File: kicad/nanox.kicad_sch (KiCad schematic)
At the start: 139 parts, among them P1 likely an ESD protection diod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, P2 likely an ESD protection diod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, P3 likely an ESD protection diod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, P4 likely an ESD protection diod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, P5 likely an ESD protection diod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, SW1 push button, left, SW2 push button, right, X1 ?, X10 TI TLV61046A boost converter 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, X11 unknown, marked AF, likely a 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, X12 unknown, likely a P-channel M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, X2 likely an N-channel MOSFET: t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, X3 likely an N-channel MOSFET: t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, X4 ?, X5 ?, X6 ?, X7 ?, X8 ?, X9 NXP PMBZ5246B 16 V Zener diod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, Y1 crystal, likely the 32 MHz HSE

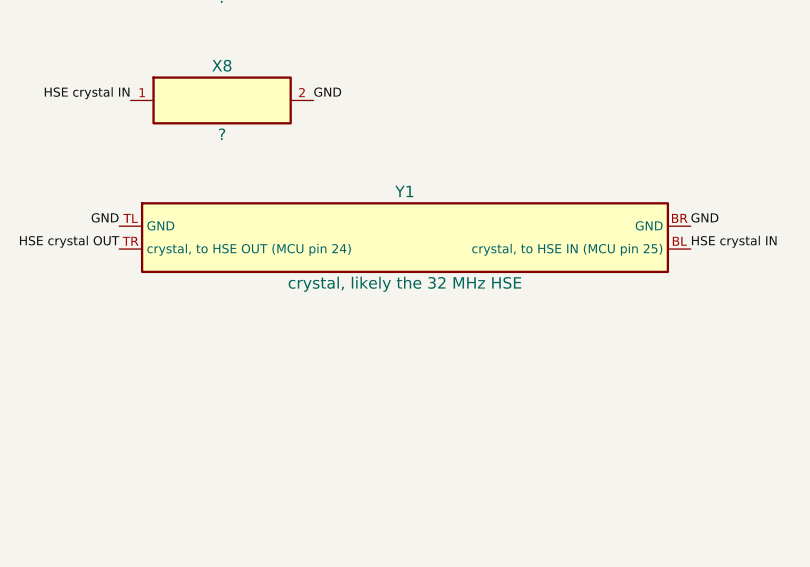
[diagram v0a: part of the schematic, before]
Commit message: Read Y1's marking as 32000 K145 Y: the 32 MHz HSE crystal, confirmed
Co-Authored-By: Claude Opus 5.5 <noreply@anthropic.com>
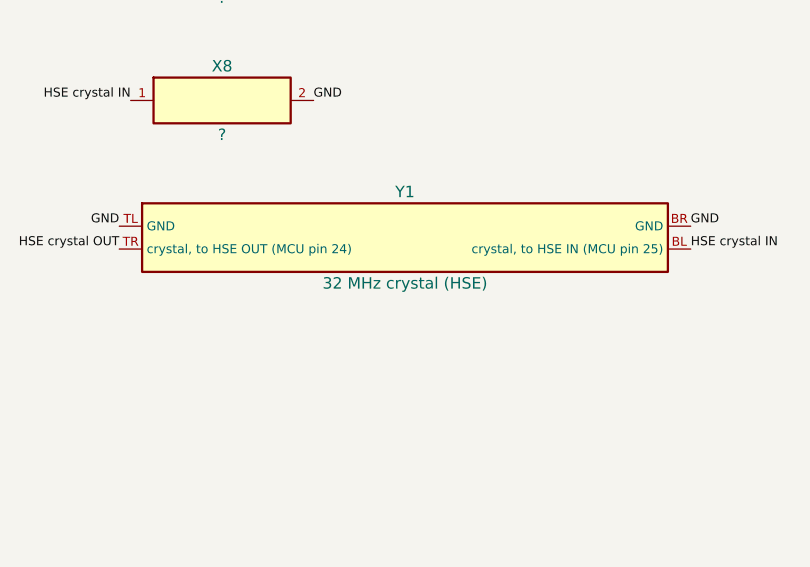
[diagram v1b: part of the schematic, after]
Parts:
- Y1: value crystal, likely the 32 MHz HSE -> 32 MHz crystal (HSE)
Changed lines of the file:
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@@
  (symbol (lib_id "nanox:Y1") (at 541.02 172.72 0) (unit 1) (in_bom yes) (on_board yes) (dnp no)
   (property "Reference" "Y1" (at 541.02 167.64 0) (effects (font (size 1.27 1.27))))
-  (property "Value" "crystal, likely the 32 MHz HSE" (at 541.02 177.80 0) (effects (font (size 1.27 1.27))))
+  (property "Value" "32 MHz crystal (HSE)" (at 541.02 177.80 0) (effects (font (size 1.27 1.27))))
   (property "Footprint" "" (at 541.02 172.72 0) (effects (font (size 1.27 1.27)) hide))
   (property "Description" "4 corner pads, ~2.0 x 1.6 mm" (at 541.02 172.72 0) (effects (font (size 1.27 1.27)) hide))

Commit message: Add the empty LSE crystal footprints as not-populated parts
The MCU's low-speed clock traces end on footprints that are left empty on
the real board: bare, solder-tinned pads for a 32.768 kHz crystal (Y2)
and its two load capacitors (C38, C39). They are now in the model, marked
DNP and excluded from the BOM in KiCad, with no 3D body, so the LSE nets
end on them and the viewers show the bare pads. The MCU must run its RTC
from its internal oscillator instead.

Co-Authored-By: Claude Opus 5.5 <noreply@anthropic.com>
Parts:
- added C38: not populated: LSE load capacitor, symbol nanox:C38
- added C39: not populated: LSE load capacitor, symbol nanox:C39
- added Y2: not populated: 32.768 kHz crystal (LSE), symbol nanox:Y2
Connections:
- net LSE crystal IN: now also C38.1, Y2.1 (LSE IN)
- net LSE crystal OUT: now also C39.1, Y2.2 (LSE OUT)
- no-connect marks 72 -> 74
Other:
- moved on the sheet: C5, C6, C7, C8, C9, L1, MCU1, P1, P2, P3, P4, P5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

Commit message: Wire L1 into the OLED boost converter and close the loose resistor and capacitor ends
- L1 gets its two pads: VIN (the pad-19 supply) and the TLV61046A's SW pin
- R24 runs to the +3.3V via below it: a pull-up on OLED SPI CS
- the +3.3V trace by R18 is straightened onto its pad: a pull-up on the
  charger's ST2 status output
- C1, C23, C24, R8 and R28 get their ground ends

Co-Authored-By: Claude Opus 5.5 <noreply@anthropic.com>
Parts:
- L1: value unknown, likely a shielded power inductor -> power inductor of the OLED boost converter
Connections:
- net +3.3V rail: now also R18.2, R24.2
- net GND: now also C1.2, C23.1, C24.1, R28.1, R8.2
- net Left button power (pad 19): now also L1.1 (VIN)
- net OLED boost SW: now also L1.2 (SW)
- no-connect marks 74 -> 67
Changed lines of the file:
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@@
  )
  (label "VBUS" (at 25.40 99.06 180) (effects (font (size 1.0 1.0)) (justify right bottom)))
- (no_connect (at 45.72 99.06))
+ (label "GND" (at 45.72 99.06 0) (effects (font (size 1.0 1.0)) (justify left bottom)))
  (symbol (lib_id "nanox:C10") (at 35.56 114.30 0) (unit 1) (in_bom yes) (on_board yes) (dnp no)
   (property "Reference" "C10" (at 35.56 110.49 0) (effects (font (size 1.27 1.27))))
@@
   (instances (project "nanox" (path "/9fc871f3-1e36-5a01-9359-e2a20c86f96f" (reference "C23") (unit 1))))
  )
- (no_connect (at 76.20 43.18))
+ (label "GND" (at 76.20 43.18 180) (effects (font (size 1.0 1.0)) (justify right bottom)))
  (label "+3.3V rail" (at 96.52 43.18 0) (effects (font (size 1.0 1.0)) (justify left bottom)))
  (symbol (lib_id "nanox:C24") (at 86.36 58.42 0) (unit 1) (in_bom yes) (on_board yes) (dnp no)
@@
   (instances (project "nanox" (path "/9fc871f3-1e36-5a01-9359-e2a20c86f96f" (reference "C24") (unit 1))))
  )
- (no_connect (at 76.20 58.42))
+ (label "GND" (at 76.20 58.42 180) (effects (font (size 1.0 1.0)) (justify right bottom)))
  (label "+3.3V rail" (at 96.52 58.42 0) (effects (font (size 1.0 1.0)) (justify left bottom)))
  (symbol (lib_id "nanox:C28") (at 86.36 73.66 0) (unit 1) (in_bom yes) (on_board yes) (dnp no)
@@
  (symbol (lib_id "nanox:L1") (at 137.16 73.66 0) (unit 1) (in_bom yes) (on_board yes) (dnp no)
   (property "Reference" "L1" (at 137.16 69.85 0) (effects (font (size 1.27 1.27))))
-  (property "Value" "unknown, likely a shielded power inductor" (at 137.16 77.47 0) (effects (font (size 1.27 1.27))))
+  (property "Value" "power inductor of the OLED boost converter" (at 137.16 77.47 0) (effects (font (size 1.27 1.27))))
   (property "Footprint" "" (at 137.16 73.66 0) (effects (font (size 1.27 1.27)) hide))
-  (property "Description" "~4.8 mm square metal" (at 137.16 73.66 0) (effects (font (size 1.27 1.27)) hide))
+  (property "Description" "~4.8 mm square metal, 2 pads" (at 137.16 73.66 0) (effects (font (size 1.27 1.27)) hide))
+  (pin "1")
+  (pin "2")
   (instances (project "nanox" (path "/9fc871f3-1e36-5a01-9359-e2a20c86f96f" (reference "L1") (unit 1))))
  )
+ (label "Left button power (pad 19)" (at 127.00 73.66 180) (effects (font (size 1.0 1.0)) (justify right bottom)))
+ (label "OLED boost SW" (at 147.32 73.66 0) (effects (font (size 1.0 1.0)) (justify left bottom)))
  (symbol (lib_id "nanox:MCU1") (at 142.24 119.38 0) (unit 1) (in_bom yes) (on_board yes) (dnp no)
   (property "Reference" "MCU1" (at 142.24 85.09 0) (effects (font (size 1.27 1.27))))
@@
  )
  (label "Charger ST2" (at 185.42 185.42 180) (effects (font (size 1.0 1.0)) (justify right bottom)))
- (no_connect (at 205.74 185.42))
+ (label "+3.3V rail" (at 205.74 185.42 0) (effects (font (size 1.0 1.0)) (justify left bottom)))
  (symbol (lib_id "nanox:R19") (at 195.58 200.66 0) (unit 1) (in_bom yes) (on_board yes) (dnp no)
   (property "Reference" "R19" (at 195.58 196.85 0) (effects (font (size 1.27 1.27))))
@@
  )
  (label "OLED SPI CS" (at 185.42 276.86 180) (effects (font (size 1.0 1.0)) (justify right bottom)))
- (no_connect (at 205.74 276.86))
+ (label "+3.3V rail" (at 205.74 276.86 0) (effects (font (size 1.0 1.0)) (justify left bottom)))
  (symbol (lib_id "nanox:R25") (at 195.58 292.10 0) (unit 1) (in_bom yes) (on_board yes) (dnp no)
   (property "Reference" "R25" (at 195.58 288.29 0) (effects (font (size 1.27 1.27))))
@@
   (instances (project "nanox" (path "/9fc871f3-1e36-5a01-9359-e2a20c86f96f" (reference "R28") (unit 1))))
  )
- (no_connect (at 236.22 58.42))
+ (label "GND" (at 236.22 58.42 180) (effects (font (size 1.0 1.0)) (justify right bottom)))
  (label "Net-T40" (at 256.54 58.42 0) (effects (font (size 1.0 1.0)) (justify left bottom)))
  (symbol (lib_id "nanox:R29") (at 246.38 73.66 0) (unit 1) (in_bom yes) (on_board yes) (dnp no)
@@
  )
  (label "Charger IEND" (at 236.22 256.54 180) (effects (font (size 1.0 1.0)) (justify right bottom)))
- (no_connect (at 256.54 256.54))
+ (label "GND" (at 256.54 256.54 0) (effects (font (size 1.0 1.0)) (justify left bottom)))
  (symbol (lib_id "nanox:R9") (at 246.38 271.78 0) (unit 1) (in_bom yes) (on_board yes) (dnp no)
   (property "Reference" "R9" (at 246.38 267.97 0) (effects (font (size 1.27 1.27))))

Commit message: Move R17 onto the I2C1 SCL trace: the clock's pull-up to +3.3V
Co-Authored-By: Claude Opus 5.5 <noreply@anthropic.com>
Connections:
- net I2C1 SCL: now also R17.2
- no-connect marks 67 -> 66
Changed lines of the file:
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@@
  )
  (label "+3.3V rail" (at 185.42 170.18 180) (effects (font (size 1.0 1.0)) (justify right bottom)))
- (no_connect (at 205.74 170.18))
+ (label "I2C1 SCL" (at 205.74 170.18 0) (effects (font (size 1.0 1.0)) (justify left bottom)))
  (symbol (lib_id "nanox:R18") (at 195.58 185.42 0) (unit 1) (in_bom yes) (on_board yes) (dnp no)
   (property "Reference" "R18" (at 195.58 181.61 0) (effects (font (size 1.27 1.27))))

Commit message: Add R36, the I2C1 SDA pull-up next to R17
The automatic pass missed it. It sits between the +3.3V trace and the end
of the SDA trace, which both already ran onto its pads.

Co-Authored-By: Claude Opus 5.5 <noreply@anthropic.com>
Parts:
- added R36: R, symbol nanox:R36
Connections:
- net +3.3V rail: now also R36.1
- net I2C1 SDA: now also R36.2
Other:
- moved on the sheet: R4, R5, R6, R7, R8, R9, RFF1, SE1, SW1, SW2, TP01, TP02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

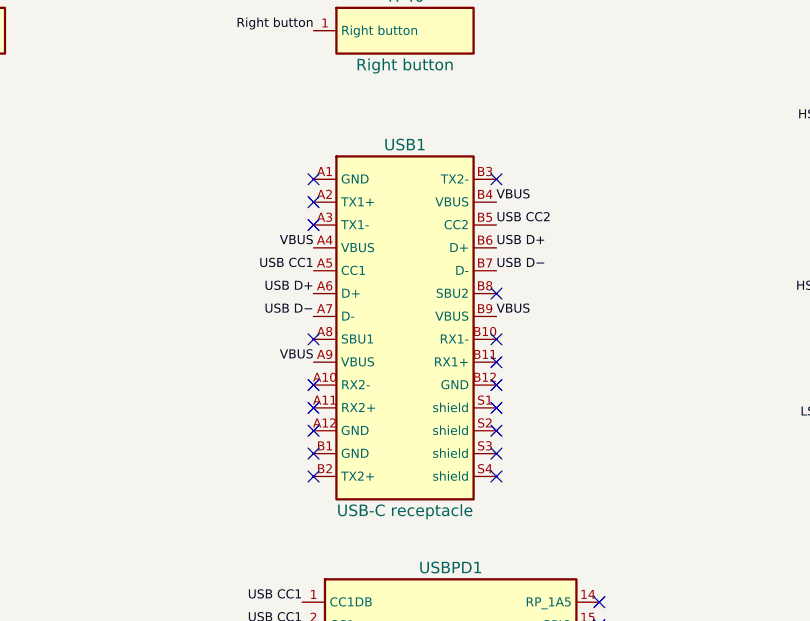
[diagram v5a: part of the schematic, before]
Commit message: Ground USB1's four GND pins (A1, A12, B1, B12) through the pour
Confirmed on the board.

Co-Authored-By: Claude Opus 5.5 <noreply@anthropic.com>
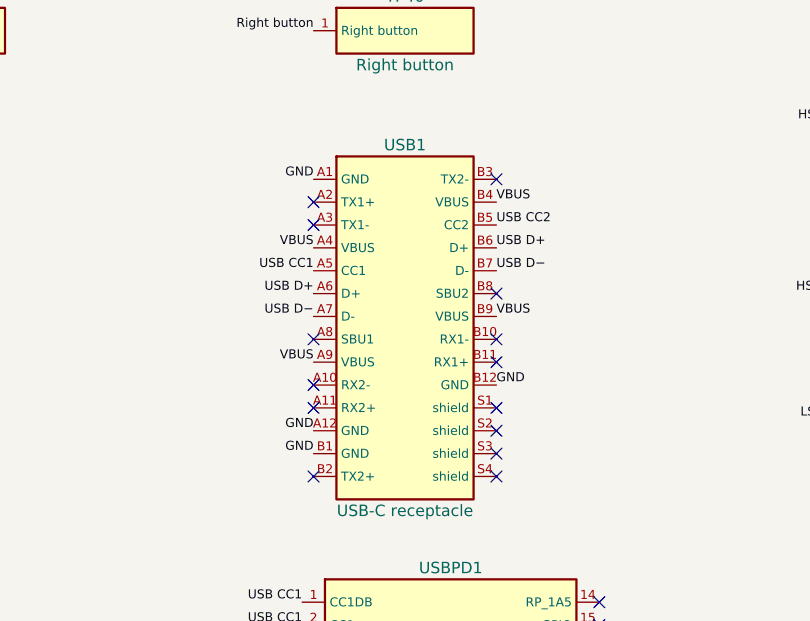
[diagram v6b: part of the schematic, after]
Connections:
- net GND: now also USB1.A1 (GND), USB1.A12 (GND), USB1.B1 (GND), USB1.B12 (GND)
- no-connect marks 66 -> 62
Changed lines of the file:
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@@
   (instances (project "nanox" (path "/9fc871f3-1e36-5a01-9359-e2a20c86f96f" (reference "USB1") (unit 1))))
  )
- (no_connect (at 436.88 181.61))
+ (label "GND" (at 436.88 181.61 180) (effects (font (size 1.0 1.0)) (justify right bottom)))
  (no_connect (at 436.88 184.15))
  (no_connect (at 436.88 186.69))
@@
  (no_connect (at 436.88 204.47))
  (no_connect (at 436.88 207.01))
- (no_connect (at 436.88 209.55))
- (no_connect (at 436.88 212.09))
+ (label "GND" (at 436.88 209.55 180) (effects (font (size 1.0 1.0)) (justify right bottom)))
+ (label "GND" (at 436.88 212.09 180) (effects (font (size 1.0 1.0)) (justify right bottom)))
  (no_connect (at 436.88 214.63))
  (no_connect (at 457.20 181.61))
@@
  (no_connect (at 457.20 199.39))
  (no_connect (at 457.20 201.93))
- (no_connect (at 457.20 204.47))
+ (label "GND" (at 457.20 204.47 0) (effects (font (size 1.0 1.0)) (justify left bottom)))
  (no_connect (at 457.20 207.01))
  (no_connect (at 457.20 209.55))

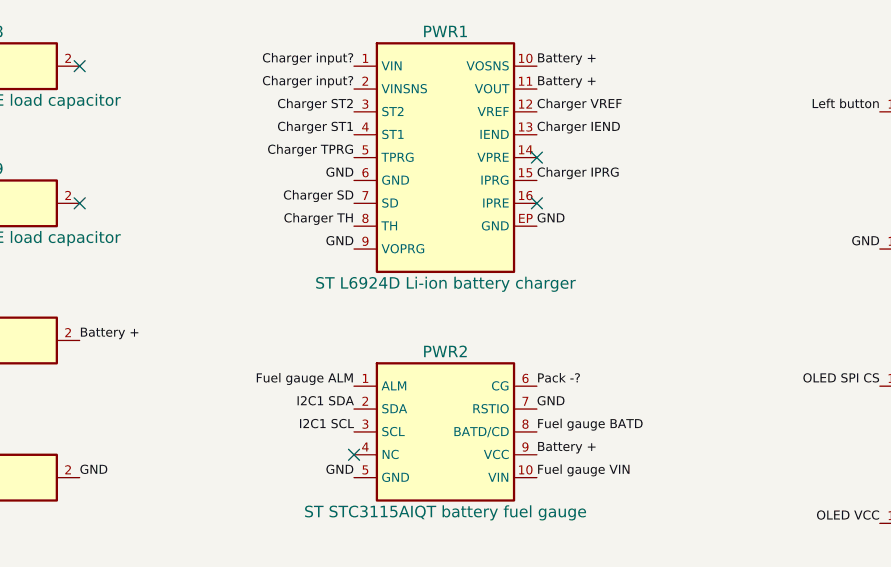
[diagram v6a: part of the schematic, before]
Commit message: Show PWR1's marking: 6924 8146
Co-Authored-By: Claude Opus 5.5 <noreply@anthropic.com>
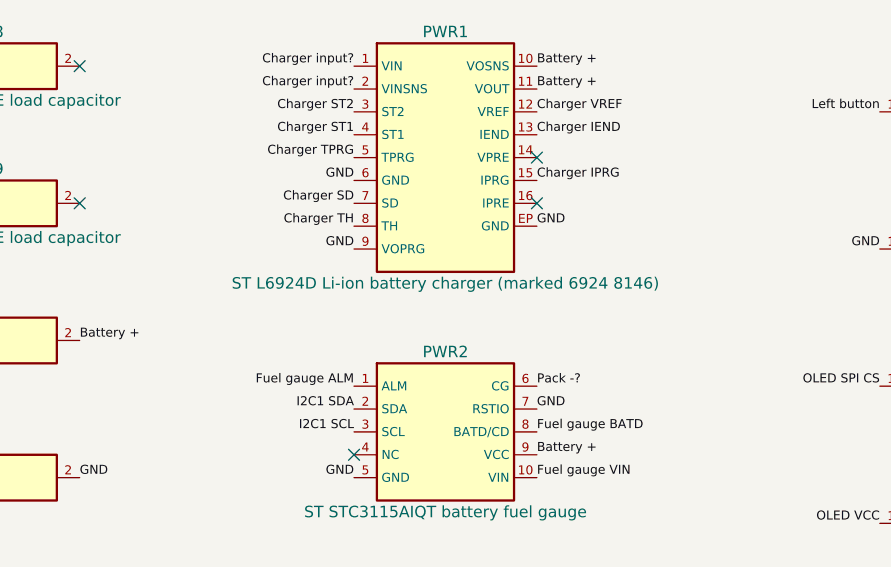
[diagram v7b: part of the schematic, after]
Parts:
- PWR1: value ST L6924D Li-ion battery charger -> ST L6924D Li-ion battery charger (marked 6924 8146)
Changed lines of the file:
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@@
  (symbol (lib_id "nanox:PWR1") (at 137.16 251.46 0) (unit 1) (in_bom yes) (on_board yes) (dnp no)
   (property "Reference" "PWR1" (at 137.16 237.49 0) (effects (font (size 1.27 1.27))))
-  (property "Value" "ST L6924D Li-ion battery charger" (at 137.16 265.43 0) (effects (font (size 1.27 1.27))))
+  (property "Value" "ST L6924D Li-ion battery charger (marked 6924 8146)" (at 137.16 265.43 0) (effects (font (size 1.27 1.27))))
   (property "Footprint" "" (at 137.16 251.46 0) (effects (font (size 1.27 1.27)) hide))
   (property "Description" "VFQFPN16, 3 x 3 mm" (at 137.16 251.46 0) (effects (font (size 1.27 1.27)) hide))

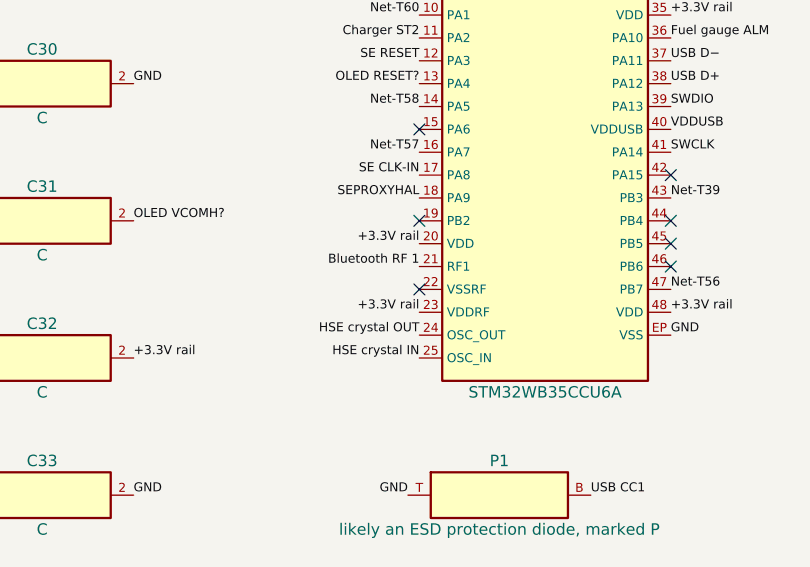
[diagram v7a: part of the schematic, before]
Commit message: Ground MCU pin 22 (VSSRF) through the pour
Co-Authored-By: Claude Opus 5.5 <noreply@anthropic.com>
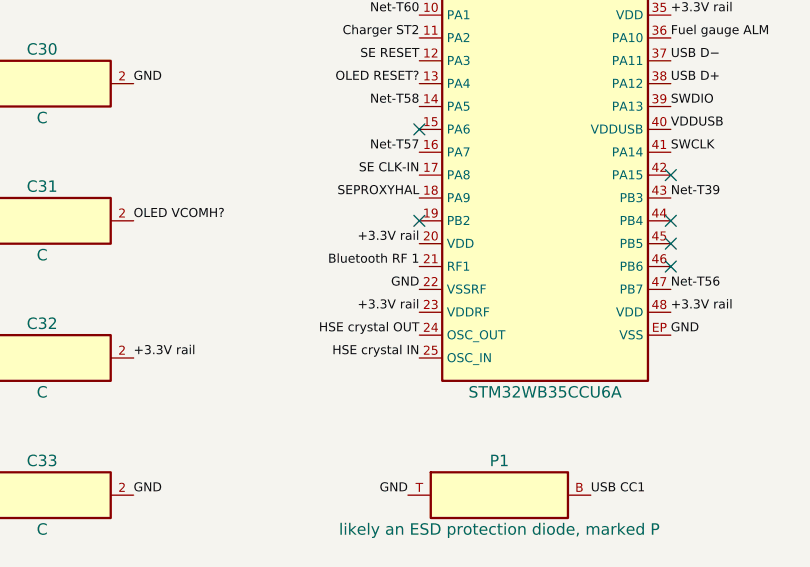
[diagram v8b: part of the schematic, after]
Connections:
- net GND: now also MCU1.22 (VSSRF)
- no-connect marks 62 -> 61
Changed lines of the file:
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@@
  (label "+3.3V rail" (at 128.27 137.16 180) (effects (font (size 1.0 1.0)) (justify right bottom)))
  (label "Bluetooth RF 1" (at 128.27 139.70 180) (effects (font (size 1.0 1.0)) (justify right bottom)))
- (no_connect (at 128.27 142.24))
+ (label "GND" (at 128.27 142.24 180) (effects (font (size 1.0 1.0)) (justify right bottom)))
  (label "+3.3V rail" (at 128.27 144.78 180) (effects (font (size 1.0 1.0)) (justify right bottom)))
  (label "HSE crystal OUT" (at 128.27 147.32 180) (effects (font (size 1.0 1.0)) (justify right bottom)))
